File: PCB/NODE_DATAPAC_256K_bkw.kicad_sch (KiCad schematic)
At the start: 28 parts, among them J1 Conn_02x20_Odd_Even, U1 74161, U10 62256, U2 74161, U3 74161, U4 74138, U5 74138, U6 74374, U7 62256, U8 62256, U9 62256

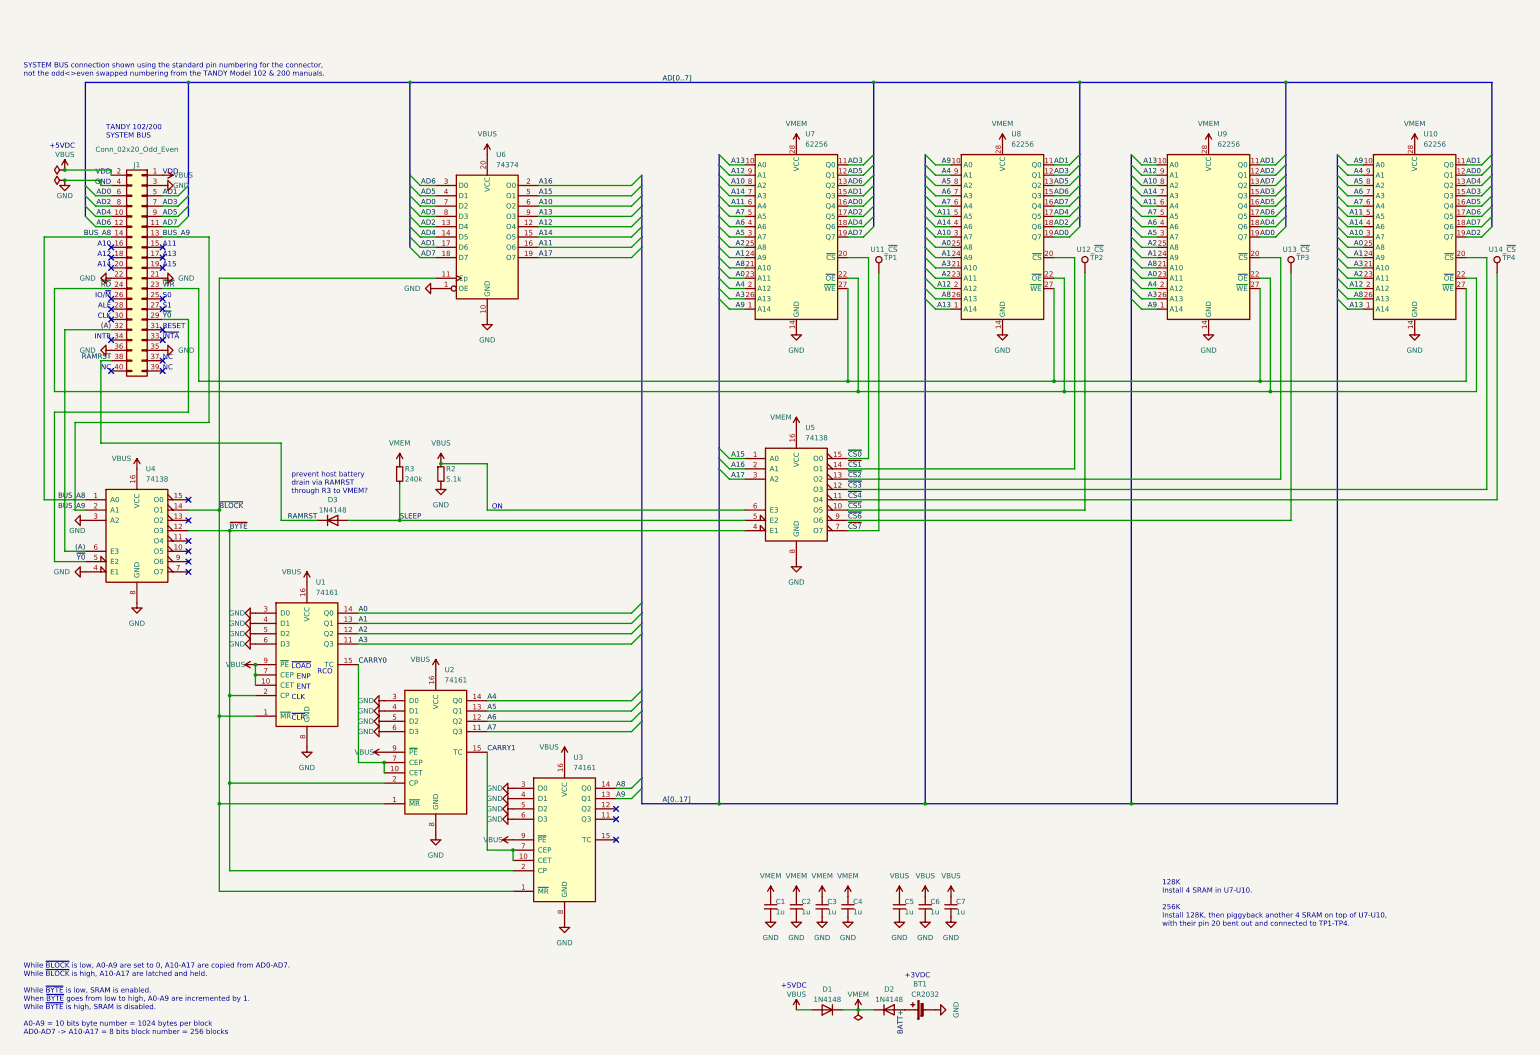
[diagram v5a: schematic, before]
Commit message: 512k support
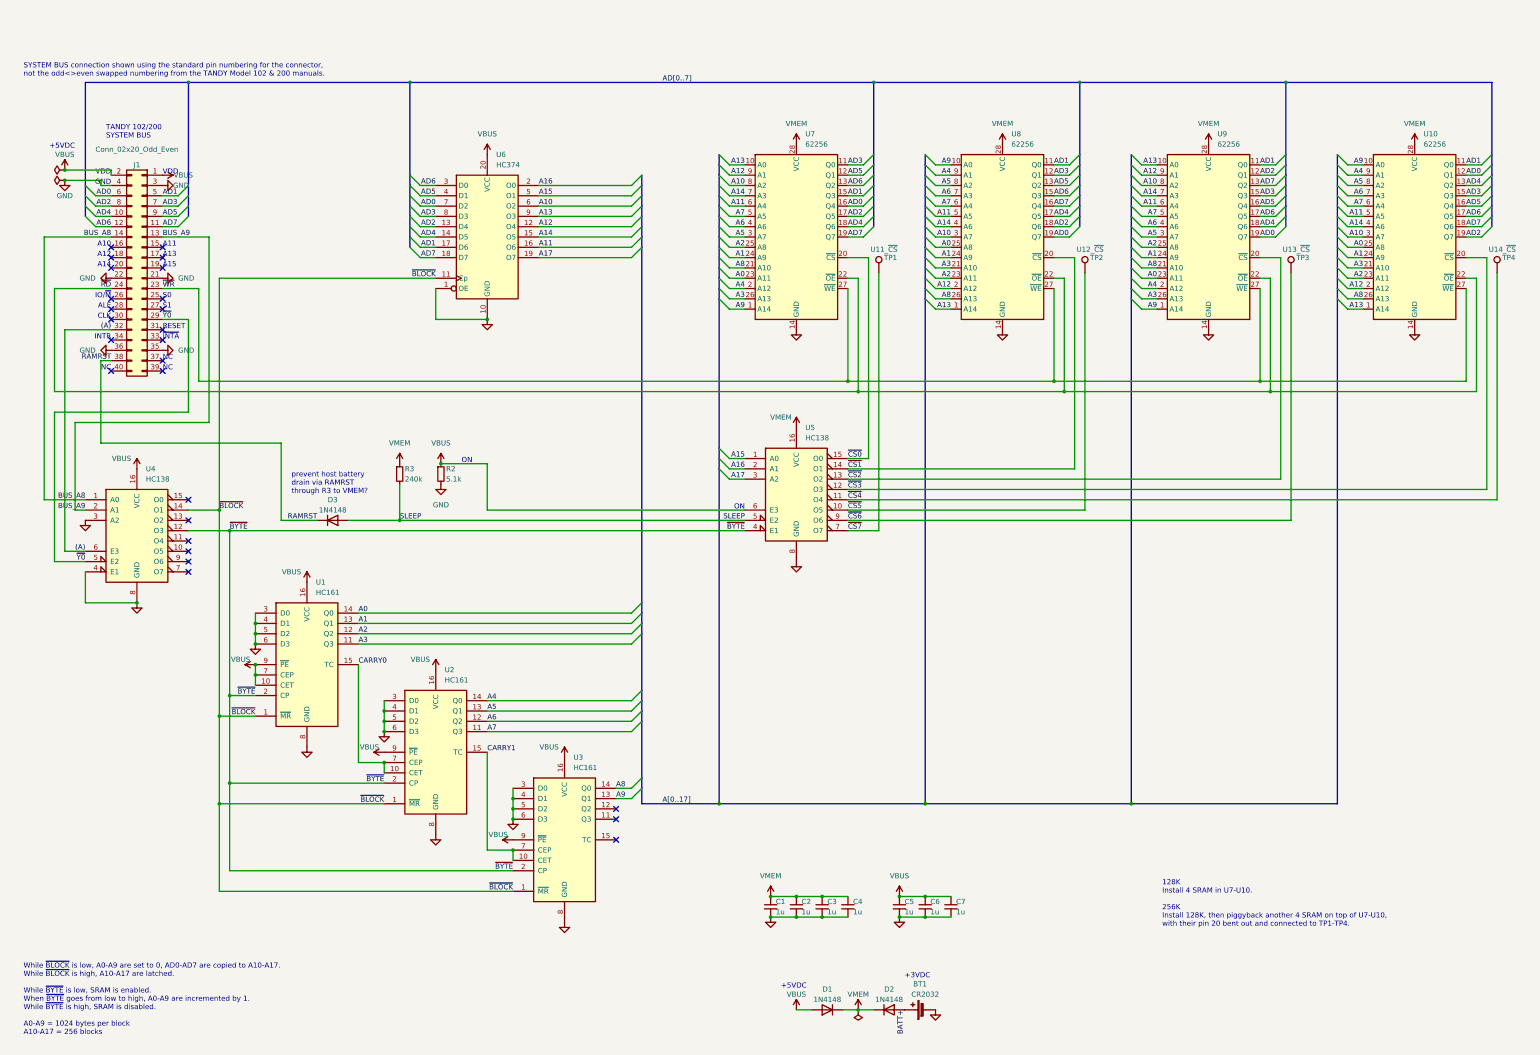
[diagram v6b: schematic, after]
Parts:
- U1, U2, U3: value 74161 -> HC161
- U4, U5: value 74138 -> HC138
- U6: value 74374 -> HC374
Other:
- note added: "While ~{BLOCK} is low, A0-A9 are set to 0, AD0-AD7 are copied to A10-A17. While ~{BLOCK} is high, A10-A17 are latched. While ~{BYTE} is low, SRAM is enabled. When ~{BYTE} goes from low to high, A0-A9 are incremented by 1. While ~{BYTE} is high, SRAM is disabled. A0-A9 = 1024 bytes per block A10-A17 = 256 blocks"
- note removed: "ENP"
- note removed: "ENT"
- note removed: "RCO"
- note removed: "While ~{BLOCK} is low, A0-A9 are set to 0, A10-A17 are copied from AD0-AD7. While ~{BLOCK} is high, A10-A17 are latched and held. While ~{BYTE} is low, SRAM is enabled. When ~{BYTE} goes from low to high, A0-A9 are incremented by 1. While ~{BYTE} is high, SRAM is disabled. A0-A9 = 10 bits byte number = 1024 bytes per block AD0-AD7 -> A10-A17 = 8 bits block number = 256 blocks"
- note removed: "~{CLR}"
- note removed: "~{LOAD}"

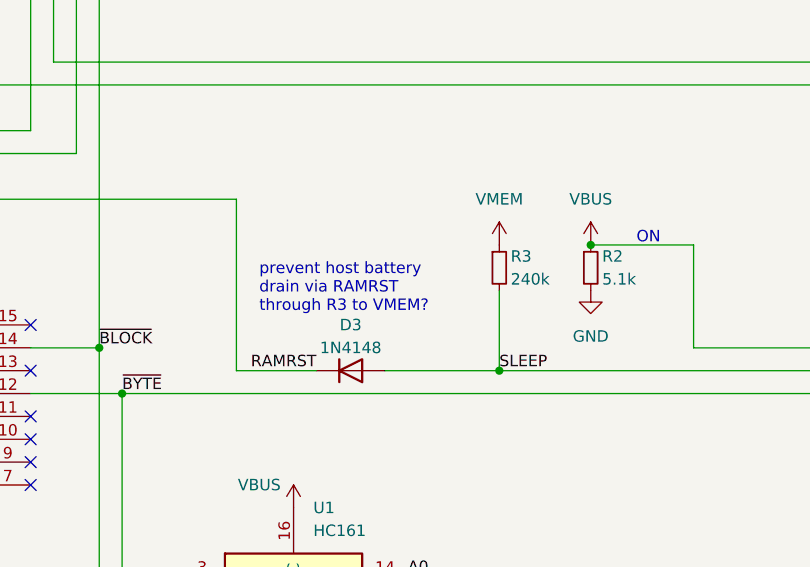
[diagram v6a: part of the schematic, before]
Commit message: notes in historical, big cap in 1M_C
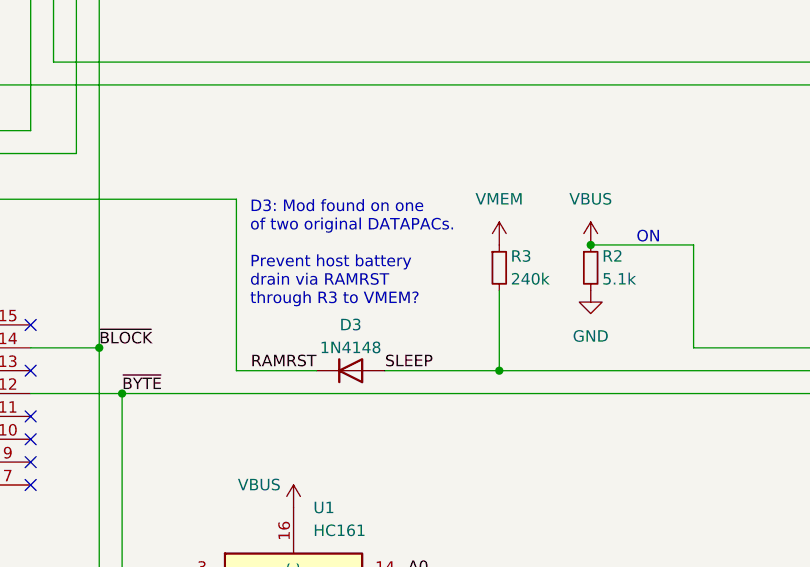
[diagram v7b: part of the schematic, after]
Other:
- note added: "D3: Mod found on one of two original DATAPACs. Prevent host battery drain via RAMRST through R3 to VMEM?"
- note removed: "prevent host battery drain via RAMRST through R3 to VMEM?"
